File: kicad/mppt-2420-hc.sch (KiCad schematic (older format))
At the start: 17 parts, among them J1 MKDS 5/ 2-9,5, J2 MKDS 5/ 2-9,5, J3 MKDS 5/ 2-9,5, J4 8P8C, J5 8P8C, J6 JST PH

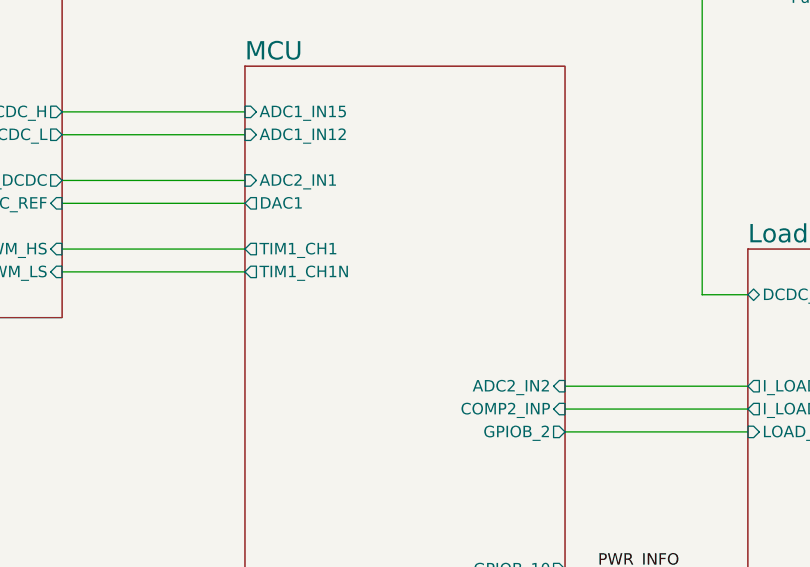
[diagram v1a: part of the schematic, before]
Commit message: Update to v0.2 with improvements after testing
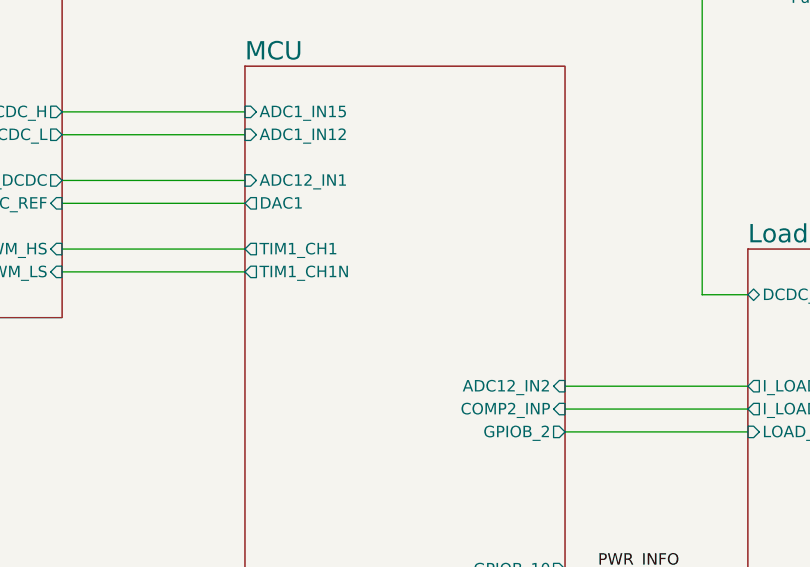
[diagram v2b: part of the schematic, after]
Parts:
- J1, J2, J3: Remarks (none) -> Alternative: DECA MB910-952M
- J4, J5: Manufacturer (none) -> Amphenol FCI; PartNumber (none) -> 54602-908LF
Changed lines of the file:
@@
 Sheet 1 6
 Title "MPPT 2420 HC"
-Date "2020-11-18"
-Rev "0.1.1"
+Date "2020-12-11"
+Rev "0.2"
 Comp "Libre Solar Technologies GmbH"
-Comment1 "Author: Martin Jäger"
-Comment2 "Website: http://libre.solar"
-Comment3 ""
+Comment1 "Website: https://libre.solar"
+Comment2 "Author: Martin Jäger"
+Comment3 "License: Creative Commons Attribution-ShareAlike 4.0 International"
 Comment4 ""
 $EndDescr
@@
 F 4 "Phoenix Contact" H 2100 2000 50  0001 C CNN "Manufacturer"
 F 5 "1714971" H 2100 2000 50  0001 C CNN "PartNumber"
+F 6 "Alternative: DECA MB910-952M" H 2100 2000 50  0001 C CNN "Remarks"
 	1    2100 2000
 	1    0    0    -1
@@
 F 4 "Phoenix Contact" H 9200 2000 50  0001 C CNN "Manufacturer"
 F 5 "1714971" H 9200 2000 50  0001 C CNN "PartNumber"
+F 6 "Alternative: DECA MB910-952M" H 9200 2000 50  0001 C CNN "Remarks"
 	1    9200 2000
 	-1   0    0    -1
@@
 F 4 "Phoenix Contact" H 9200 3400 50  0001 C CNN "Manufacturer"
 F 5 "1714971" H 9200 3400 50  0001 C CNN "PartNumber"
+F 6 "Alternative: DECA MB910-952M" H 9200 3400 50  0001 C CNN "Remarks"
 	1    9200 3400
 	-1   0    0    -1
@@
 F5 "ADC1_IN15" I L 5200 2500 50
 F6 "ADC1_IN12" I L 5200 2600 50
-F7 "ADC2_IN1" I L 5200 2800 50
-F8 "ADC2_IN2" I R 6600 3700 50
-F9 "FDCAN1_RX" I L 5200 5200 50
-F10 "FDCAN1_TX" O L 5200 5100 50
-F11 "TIM8_CH2" O R 6600 5900 50
-F12 "COMP2_INP" I R 6600 3800 50
-F13 "GPIOB_11" O L 5200 5500 50
-F14 "GPIOB_2" O R 6600 3900 50
-F15 "GPIOB_10" O R 6600 4500 50
+F7 "FDCAN1_RX" I L 5200 5200 50
+F8 "FDCAN1_TX" O L 5200 5100 50
+F9 "TIM8_CH2" O R 6600 5900 50
+F10 "COMP2_INP" I R 6600 3800 50
+F11 "GPIOB_11" O L 5200 5500 50
+F12 "GPIOB_2" O R 6600 3900 50
+F13 "GPIOB_10" O R 6600 4500 50
+F14 "ADC12_IN1" I L 5200 2800 50
+F15 "ADC12_IN2" I R 6600 3700 50
 $EndSheet
 $Comp
@@
 F 3 "" V 1600 5425 50  0001 C CNN
 F 4 "+can" H 1600 5400 50  0001 C CNN "Config"
+F 5 "Amphenol FCI" H 1600 5400 50  0001 C CNN "Manufacturer"
+F 6 "54602-908LF" H 1600 5400 50  0001 C CNN "PartNumber"
 	1    1600 5400
 	1    0    0    1
@@
 F 3 "" V 1600 4125 50  0001 C CNN
 F 4 "+can" H 1600 4100 50  0001 C CNN "Config"
+F 5 "Amphenol FCI" H 1600 4100 50  0001 C CNN "Manufacturer"
+F 6 "54602-908LF" H 1600 4100 50  0001 C CNN "PartNumber"
 	1    1600 4100
 	1    0    0    1

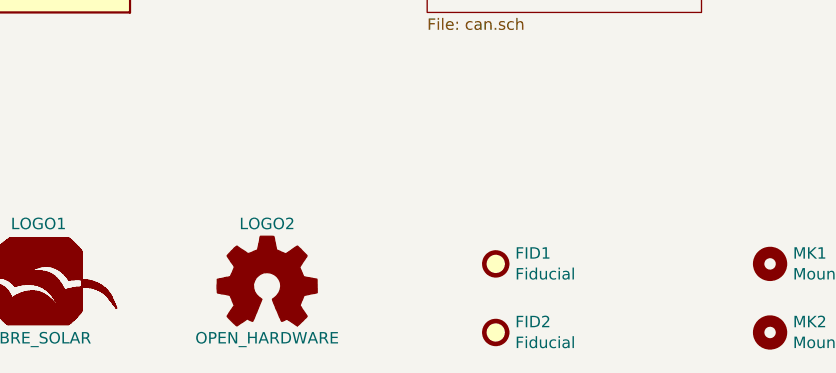
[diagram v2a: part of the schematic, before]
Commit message: Minor updates for v0.2.1
Adjustments in silk screen and second bulk output cap.
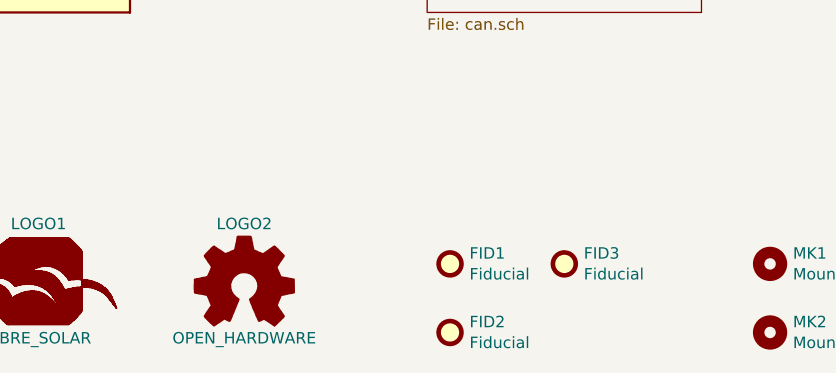
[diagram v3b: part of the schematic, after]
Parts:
- added FID3: Fiducial, LibreSolar:Fiducial_0.7mm, symbol Mechanical:Fiducial
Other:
- moved on the sheet: FID1, FID2, LOGO2
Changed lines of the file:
@@
 Sheet 1 6
 Title "MPPT 2420 HC"
-Date "2020-12-11"
-Rev "0.2"
+Date "2021-01-06"
+Rev "0.2.1"
 Comp "Libre Solar Technologies GmbH"
 Comment1 "Website: https://libre.solar"
@@
 L Graphic:Logo_Open_Hardware_Small LOGO2
 U 1 1 58C36283
-P 2500 7100
-F 0 "LOGO2" H 2500 7375 50  0000 C CNN
-F 1 "OPEN_HARDWARE" H 2500 6875 50  0000 C CNN
-F 2 "Symbol:OSHW-Logo_5.7x6mm_SilkScreen" H 2500 7100 60  0001 C CNN
-F 3 "" H 2500 7100 60  0001 C CNN
-F 4 "+info" H 2500 7100 50  0001 C CNN "Config"
-	1    2500 7100
+P 2400 7100
+F 0 "LOGO2" H 2400 7375 50  0000 C CNN
+F 1 "OPEN_HARDWARE" H 2400 6875 50  0000 C CNN
+F 2 "Symbol:OSHW-Logo_5.7x6mm_SilkScreen" H 2400 7100 60  0001 C CNN
+F 3 "" H 2400 7100 60  0001 C CNN
+F 4 "+info" H 2400 7100 50  0001 C CNN "Config"
+	1    2400 7100
 	1    0    0    -1
 $EndComp
@@
 L Mechanical:Fiducial FID1
 U 1 1 5D9CC06F
-P 3500 7000
-F 0 "FID1" H 3585 7046 50  0000 L CNN
-F 1 "Fiducial" H 3585 6955 50  0000 L CNN
-F 2 "LibreSolar:Fiducial_0.7mm" H 3500 7000 50  0001 C CNN
-F 3 "~" H 3500 7000 50  0001 C CNN
-F 4 "+info" H 3500 7000 50  0001 C CNN "Config"
-	1    3500 7000
+P 3300 7000
+F 0 "FID1" H 3385 7046 50  0000 L CNN
+F 1 "Fiducial" H 3385 6955 50  0000 L CNN
+F 2 "LibreSolar:Fiducial_0.7mm" H 3300 7000 50  0001 C CNN
+F 3 "~" H 3300 7000 50  0001 C CNN
+F 4 "+info" H 3300 7000 50  0001 C CNN "Config"
+	1    3300 7000
 	1    0    0    -1
 $EndComp
@@
 L Mechanical:Fiducial FID2
 U 1 1 5D9CC750
-P 3500 7300
-F 0 "FID2" H 3585 7346 50  0000 L CNN
-F 1 "Fiducial" H 3585 7255 50  0000 L CNN
-F 2 "LibreSolar:Fiducial_0.7mm" H 3500 7300 50  0001 C CNN
-F 3 "~" H 3500 7300 50  0001 C CNN
-F 4 "+info" H 3500 7300 50  0001 C CNN "Config"
-	1    3500 7300
+P 3300 7300
+F 0 "FID2" H 3385 7346 50  0000 L CNN
+F 1 "Fiducial" H 3385 7255 50  0000 L CNN
+F 2 "LibreSolar:Fiducial_0.7mm" H 3300 7300 50  0001 C CNN
+F 3 "~" H 3300 7300 50  0001 C CNN
+F 4 "+info" H 3300 7300 50  0001 C CNN "Config"
+	1    3300 7300
 	1    0    0    -1
 $EndComp
@@
 Wire Wire Line
 	9300 4900 9800 4900
+$Comp
+L Mechanical:Fiducial FID3
+U 1 1 5FFCD2A9
+P 3800 7000
+F 0 "FID3" H 3885 7046 50  0000 L CNN
+F 1 "Fiducial" H 3885 6955 50  0000 L CNN
+F 2 "LibreSolar:Fiducial_0.7mm" H 3800 7000 50  0001 C CNN
+F 3 "~" H 3800 7000 50  0001 C CNN
+F 4 "+info" H 3800 7000 50  0001 C CNN "Config"
+	1    3800 7000
+	1    0    0    -1
+$EndComp
 $EndSCHEMATC
